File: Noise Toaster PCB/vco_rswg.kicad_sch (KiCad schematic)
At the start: 21 parts, among them Q1 2N5457, U1 LM324, U2 LM324

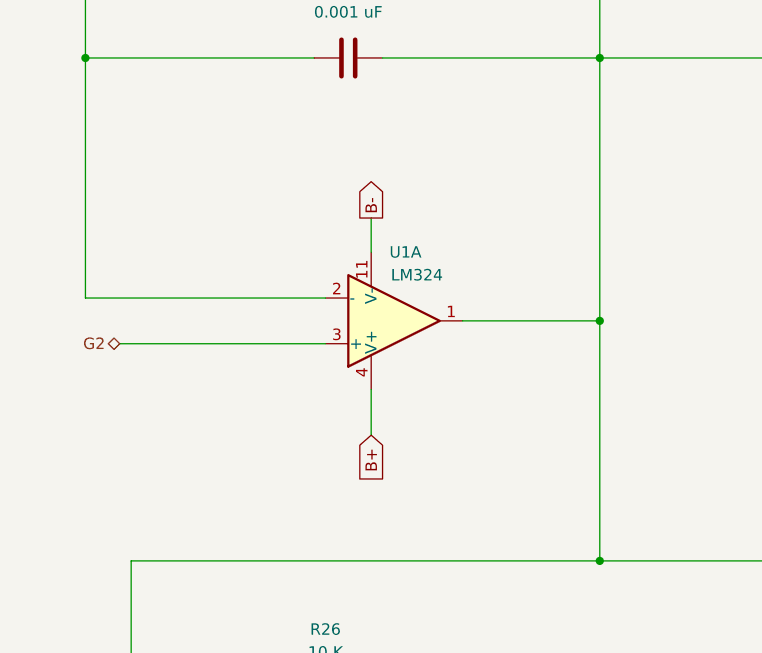
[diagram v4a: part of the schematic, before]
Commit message: applied footprints
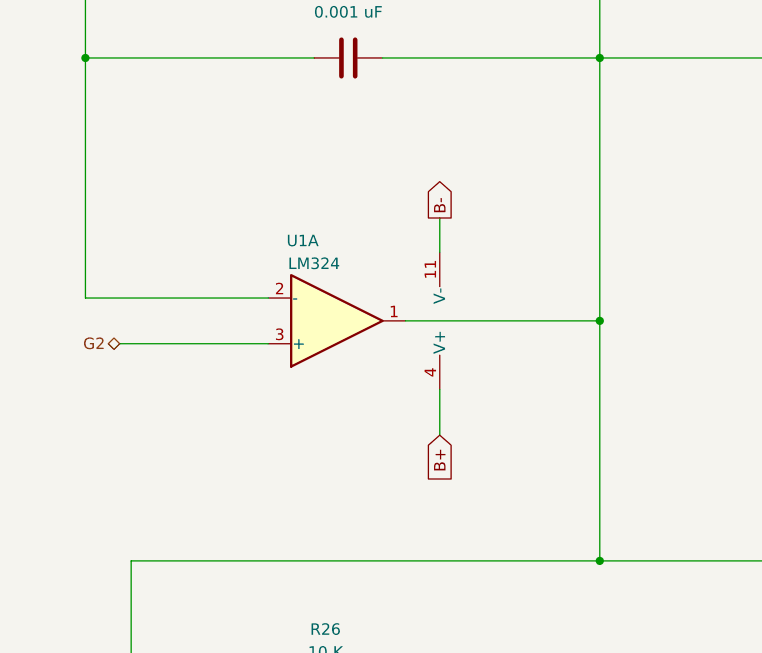
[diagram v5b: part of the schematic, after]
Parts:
- C11, C2, C6: footprint (none) -> Capacitor_THT:C_Disc_D5.1mm_W3.2mm_P5.00mm
- D1: footprint (none) -> Diode_THT:D_DO-35_SOD27_P7.62mm_Horizontal
- Q1: footprint (none) -> Package_TO_SOT_THT:TO-92_Inline
- R12, R17, R18, R24, R26, R30, R31, R32, R5, R6, R7: footprint (none) -> Resistor_THT:R_Axial_DIN0207_L6.3mm_D2.5mm_P10.16mm_Horizontal
- U1, U2: footprint (none) -> Package_DIP:DIP-14_W7.62mm_Socket
- X4: footprint (none) -> Connector_PinHeader_1.00mm:PinHeader_1x01_P1.00mm_Vertical
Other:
- moved on the sheet: U1A
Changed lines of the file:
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@@
     (stroke (width 0) (type default))
   )
-  (wire (pts (xy 63.5 100.33) (xy 63.5 105.41))
+  (wire (pts (xy 71.12 100.33) (xy 71.12 105.41))
     (stroke (width 0) (type default))
   )
@@
     (stroke (width 0) (type default))
   )
-  (wire (pts (xy 73.66 92.71) (xy 88.9 92.71))
+  (wire (pts (xy 67.31 92.71) (xy 88.9 92.71))
     (stroke (width 0) (type default))
   )
@@
     (stroke (width 0) (type default))
   )
-  (wire (pts (xy 35.56 95.25) (xy 58.42 95.25))
+  (wire (pts (xy 35.56 95.25) (xy 52.07 95.25))
     (stroke (width 0) (type default))
   )
@@
     (stroke (width 0) (type default))
   )
-  (wire (pts (xy 31.75 90.17) (xy 58.42 90.17))
+  (wire (pts (xy 31.75 90.17) (xy 52.07 90.17))
     (stroke (width 0) (type default))
   )
@@
     (stroke (width 0) (type default))
   )
-  (wire (pts (xy 63.5 81.28) (xy 63.5 85.09))
+  (wire (pts (xy 71.12 81.28) (xy 71.12 85.09))
     (stroke (width 0) (type default))
   )
@@
     )
   )
-  (global_label "B-" (shape output) (at 63.5 81.28 90) (fields_autoplaced)
+  (global_label "B-" (shape output) (at 71.12 81.28 90) (fields_autoplaced)
     (effects (font (size 1.27 1.27)) (justify left))
-    (property "Intersheetrefs" "${INTERSHEET_REFS}" (at 63.5 75.4524 90)
+    (property "Intersheetrefs" "${INTERSHEET_REFS}" (at 71.12 75.4524 90)
       (effects (font (size 1.27 1.27)) (justify left) hide)
     )
   )
-  (global_label "B+" (shape input) (at 63.5 105.41 270) (fields_autoplaced)
+  (global_label "B+" (shape input) (at 71.12 105.41 270) (fields_autoplaced)
     (effects (font (size 1.27 1.27)) (justify right))
-    (property "Intersheetrefs" "${INTERSHEET_REFS}" (at 63.5 111.2376 90)
+    (property "Intersheetrefs" "${INTERSHEET_REFS}" (at 71.12 111.2376 90)
       (effects (font (size 1.27 1.27)) (justify right) hide)
     )
@@
       (effects (font (size 1.27 1.27)))
     )
-    (property "Footprint" "" (at 95.25 143.51 0)
+    (property "Footprint" "Package_DIP:DIP-14_W7.62mm_Socket" (at 95.25 143.51 0)
       (effects (font (size 1.27 1.27)) hide)
     )
@@
       (effects (font (size 1.27 1.27)))
     )
-    (property "Footprint" "" (at 246.38 133.35 0)
+    (property "Footprint" "Connector_PinHeader_1.00mm:PinHeader_1x01_P1.00mm_Vertical" (at 246.38 133.35 0)
       (effects (font (size 1.27 1.27)) hide)
     )
@@
       (effects (font (size 1.27 1.27)))
     )
-    (property "Footprint" "" (at 196.85 63.5 0)
+    (property "Footprint" "Package_DIP:DIP-14_W7.62mm_Socket" (at 196.85 63.5 0)
       (effects (font (size 1.27 1.27)) hide)
     )
@@
       (effects (font (size 1.27 1.27)))
     )
-    (property "Footprint" "" (at 58.42 150.368 90)
+    (property "Footprint" "Resistor_THT:R_Axial_DIN0207_L6.3mm_D2.5mm_P10.16mm_Horizontal" (at 58.42 150.368 90)
       (effects (font (size 1.27 1.27)) hide)
     )
@@
       (effects (font (size 1.27 1.27)))
     )
-    (property "Footprint" "" (at 123.19 27.178 90)
+    (property "Footprint" "Resistor_THT:R_Axial_DIN0207_L6.3mm_D2.5mm_P10.16mm_Horizontal" (at 123.19 27.178 90)
       (effects (font (size 1.27 1.27)) hide)
     )
@@
       (effects (font (size 1.27 1.27)))
     )
-    (property "Footprint" "" (at 215.9 103.378 90)
+    (property "Footprint" "Resistor_THT:R_Axial_DIN0207_L6.3mm_D2.5mm_P10.16mm_Horizontal" (at 215.9 103.378 90)
       (effects (font (size 1.27 1.27)) hide)
     )
@@
       (effects (font (size 1.27 1.27)))
     )
-    (property "Footprint" "" (at 158.75 25.4 0)
+    (property "Footprint" "Diode_THT:D_DO-35_SOD27_P7.62mm_Horizontal" (at 158.75 25.4 0)
       (effects (font (size 1.27 1.27)) hide)
     )
@@
       (effects (font (size 1.27 1.27)))
     )
-    (property "Footprint" "" (at 215.9 119.888 90)
+    (property "Footprint" "Resistor_THT:R_Axial_DIN0207_L6.3mm_D2.5mm_P10.16mm_Horizontal" (at 215.9 119.888 90)
       (effects (font (size 1.27 1.27)) hide)
     )
@@
       (effects (font (size 1.27 1.27)))
     )
-    (property "Footprint" "" (at 114.3 95.25 0)
+    (property "Footprint" "Connector_PinHeader_1.00mm:PinHeader_1x01_P1.00mm_Vertical" (at 114.3 95.25 0)
       (effects (font (size 1.27 1.27)) hide)
     )
@@
       (effects (font (size 1.27 1.27)))
     )
-    (property "Footprint" "" (at 203.2 46.228 90)
+    (property "Footprint" "Resistor_THT:R_Axial_DIN0207_L6.3mm_D2.5mm_P10.16mm_Horizontal" (at 203.2 46.228 90)
       (effects (font (size 1.27 1.27)) hide)
     )
@@
       (effects (font (size 1.27 1.27)))
     )
-    (property "Footprint" "" (at 185.42 135.128 90)
+    (property "Footprint" "Resistor_THT:R_Axial_DIN0207_L6.3mm_D2.5mm_P10.16mm_Horizontal" (at 185.42 135.128 90)
       (effects (font (size 1.27 1.27)) hide)
     )
@@
       (effects (font (size 1.27 1.27)))
     )
-    (property "Footprint" "" (at 123.19 39.878 90)
+    (property "Footprint" "Resistor_THT:R_Axial_DIN0207_L6.3mm_D2.5mm_P10.16mm_Horizontal" (at 123.19 39.878 90)
       (effects (font (size 1.27 1.27)) hide)
     )
@@
       (effects (font (size 1.27 1.27)))
     )
-    (property "Footprint" "" (at 58.42 133.858 90)
+    (property "Footprint" "Resistor_THT:R_Axial_DIN0207_L6.3mm_D2.5mm_P10.16mm_Horizontal" (at 58.42 133.858 90)
       (effects (font (size 1.27 1.27)) hide)
     )
@@
       (effects (font (size 1.27 1.27)))
     )
-    (property "Footprint" "" (at 62.23 176.8348 0)
+    (property "Footprint" "Capacitor_THT:C_Disc_D5.1mm_W3.2mm_P5.00mm" (at 62.23 176.8348 0)
       (effects (font (size 1.27 1.27)) hide)
     )
@@
       (effects (font (size 1.27 1.27)))
     )
-    (property "Footprint" "" (at 185.42 149.098 90)
+    (property "Footprint" "Resistor_THT:R_Axial_DIN0207_L6.3mm_D2.5mm_P10.16mm_Horizontal" (at 185.42 149.098 90)
       (effects (font (size 1.27 1.27)) hide)
     )
@@
       (effects (font (size 1.27 1.27)) (justify right))
     )
-    (property "Footprint" "" (at 164.1348 96.52 0)
+    (property "Footprint" "Capacitor_THT:C_Disc_D5.1mm_W3.2mm_P5.00mm" (at 164.1348 96.52 0)
       (effects (font (size 1.27 1.27)) hide)
     )
@@
       (effects (font (size 1.27 1.27)))
     )
-    (property "Footprint" "" (at 64.77 62.5348 0)
+    (property "Footprint" "Capacitor_THT:C_Disc_D5.1mm_W3.2mm_P5.00mm" (at 64.77 62.5348 0)
       (effects (font (size 1.27 1.27)) hide)
     )
@@
     )
   )
-  (symbol (lib_id "Amplifier_Operational:LM324") (at 66.04 92.71 0) (mirror x) (unit 1)
-    (in_bom yes) (on_board yes) (dnp no)
-    (property "Reference" "U1" (at 67.31 85.09 0)
-      (effects (font (size 1.27 1.27)))
-    )
-    (property "Value" "LM324" (at 68.58 87.63 0)
-      (effects (font (size 1.27 1.27)))
-    )
-    (property "Footprint" "" (at 64.77 95.25 0)
-      (effects (font (size 1.27 1.27)) hide)
-    )
-    (property "Datasheet" "http://www.ti.com/lit/ds/symlink/lm2902-n.pdf" (at 67.31 97.79 0)
+  (symbol (lib_id "Amplifier_Operational:LM324") (at 59.69 92.71 0) (mirror x) (unit 1)
+    (in_bom yes) (on_board yes) (dnp no)
+    (property "Reference" "U1" (at 55.88 83.82 0)
+      (effects (font (size 1.27 1.27)))
+    )
+    (property "Value" "LM324" (at 57.15 86.36 0)
+      (effects (font (size 1.27 1.27)))
+    )
+    (property "Footprint" "Package_DIP:DIP-14_W7.62mm_Socket" (at 58.42 95.25 0)
+      (effects (font (size 1.27 1.27)) hide)
+    )
+    (property "Datasheet" "http://www.ti.com/lit/ds/symlink/lm2902-n.pdf" (at 60.96 97.79 0)
       (effects (font (size 1.27 1.27)) hide)
     )
@@
       (effects (font (size 1.27 1.27)))
     )
-    (property "Footprint" "" (at 124.46 65.278 90)
+    (property "Footprint" "Resistor_THT:R_Axial_DIN0207_L6.3mm_D2.5mm_P10.16mm_Horizontal" (at 124.46 65.278 90)
       (effects (font (size 1.27 1.27)) hide)
     )
@@
       (effects (font (size 1.27 1.27)))
     )
-    (property "Footprint" "" (at 58.42 43.18 0)
+    (property "Footprint" "Package_TO_SOT_THT:TO-92_Inline" (at 58.42 43.18 0)
       (effects (font (size 1.27 1.27)) hide)
     )
@@
       (effects (font (size 1.27 1.27)))
     )
-    (property "Footprint" "" (at 127 119.38 0)
+    (property "Footprint" "Connector_PinHeader_1.00mm:PinHeader_1x01_P1.00mm_Vertical" (at 127 119.38 0)
       (effects (font (size 1.27 1.27)) hide)
     )
@@
     )
   )
-  (symbol (lib_id "Amplifier_Operational:LM324") (at 60.96 92.71 180) (unit 5)
-    (in_bom yes) (on_board yes) (dnp no)
-    (property "Reference" "U1" (at 64.77 91.44 0)
+  (symbol (lib_id "Amplifier_Operational:LM324") (at 68.58 92.71 180) (unit 5)
+    (in_bom yes) (on_board yes) (dnp no)
+    (property "Reference" "U1" (at 72.39 91.44 0)
       (effects (font (size 1.27 1.27)) (justify right) hide)
     )
-    (property "Value" "LM324" (at 67.31 96.52 0)
+    (property "Value" "LM324" (at 74.93 96.52 0)
       (effects (font (size 1.27 1.27)) (justify right) hide)
     )
-    (property "Footprint" "" (at 62.23 95.25 0)
-      (effects (font (size 1.27 1.27)) hide)
-    )
-    (property "Datasheet" "http://www.ti.com/lit/ds/symlink/lm2902-n.pdf" (at 59.69 97.79 0)
+    (property "Footprint" "Package_DIP:DIP-14_W7.62mm_Socket" (at 69.85 95.25 0)
+      (effects (font (size 1.27 1.27)) hide)
+    )
+    (property "Datasheet" "http://www.ti.com/lit/ds/symlink/lm2902-n.pdf" (at 67.31 97.79 0)
       (effects (font (size 1.27 1.27)) hide)
     )
@@
       (effects (font (size 1.27 1.27)))
     )
-    (property "Footprint" "" (at 215.9 84.328 90)
-      (effects (font (size 1.27 1.27)) hide)
-    )
+    (property "Footprint" "Resistor_THT:R_Axial_DIN0207_L6.3mm_D2.5mm_P10.16mm_Horizontal" (at 215.9 84.328 90)
+      (effects (font (size 1.27 1.27)) hide)
+    )

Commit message: placed pards of the pcb properly
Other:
- company: http://musicfromouterspace.com/analogsynth_new/NOISETOASTER/NOISETOASTER.php -> Music From Outer Space LLC
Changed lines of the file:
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@@
     (title "VCO - Ramp/Square Wave Generator")
     (rev "0.5")
-    (company "http://musicfromouterspace.com/analogsynth_new/NOISETOASTER/NOISETOASTER.php")
+    (company "Music From Outer Space LLC")
     (comment 1 "Licence: CC-BY-NC-SA")
     (comment 2 "Original Design by Ray Wilson")
-    (comment 3 "Music From Outer Space LLC")
+    (comment 3 "http://musicfromouterspace.com/analogsynth_new/NOISETOASTER/NOISETOASTER.php")
   )
   (junction (at 165.1 118.11) (diameter 0) (color 0 0 0 0)

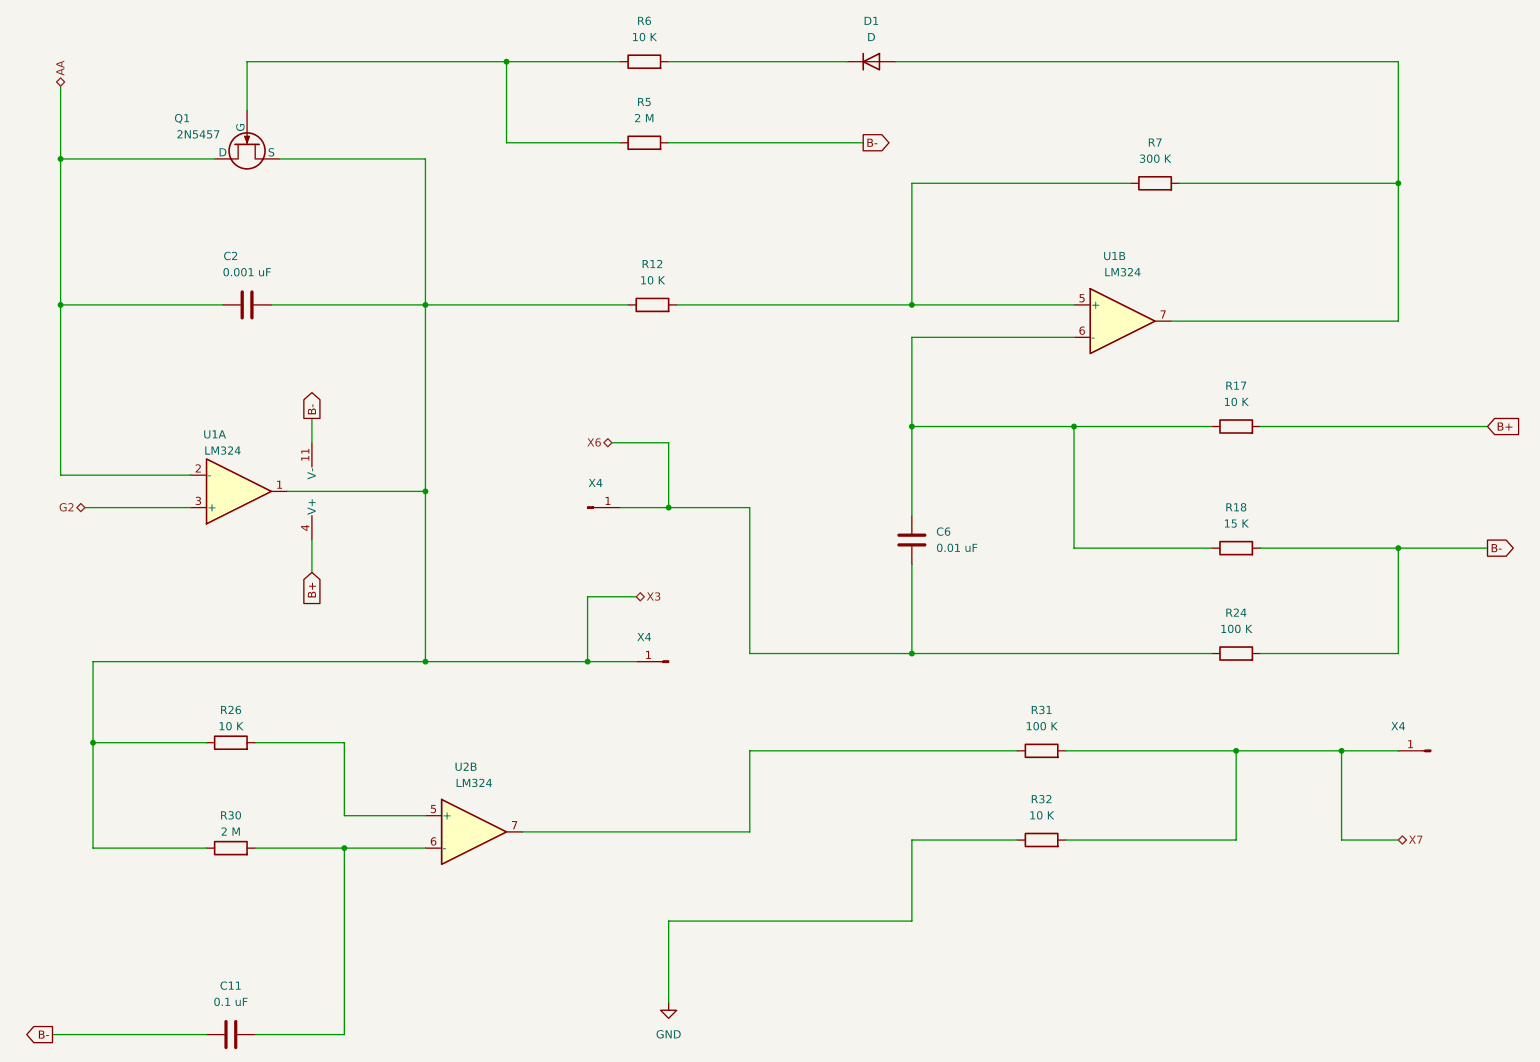
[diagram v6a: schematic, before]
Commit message: changed header pins to groups
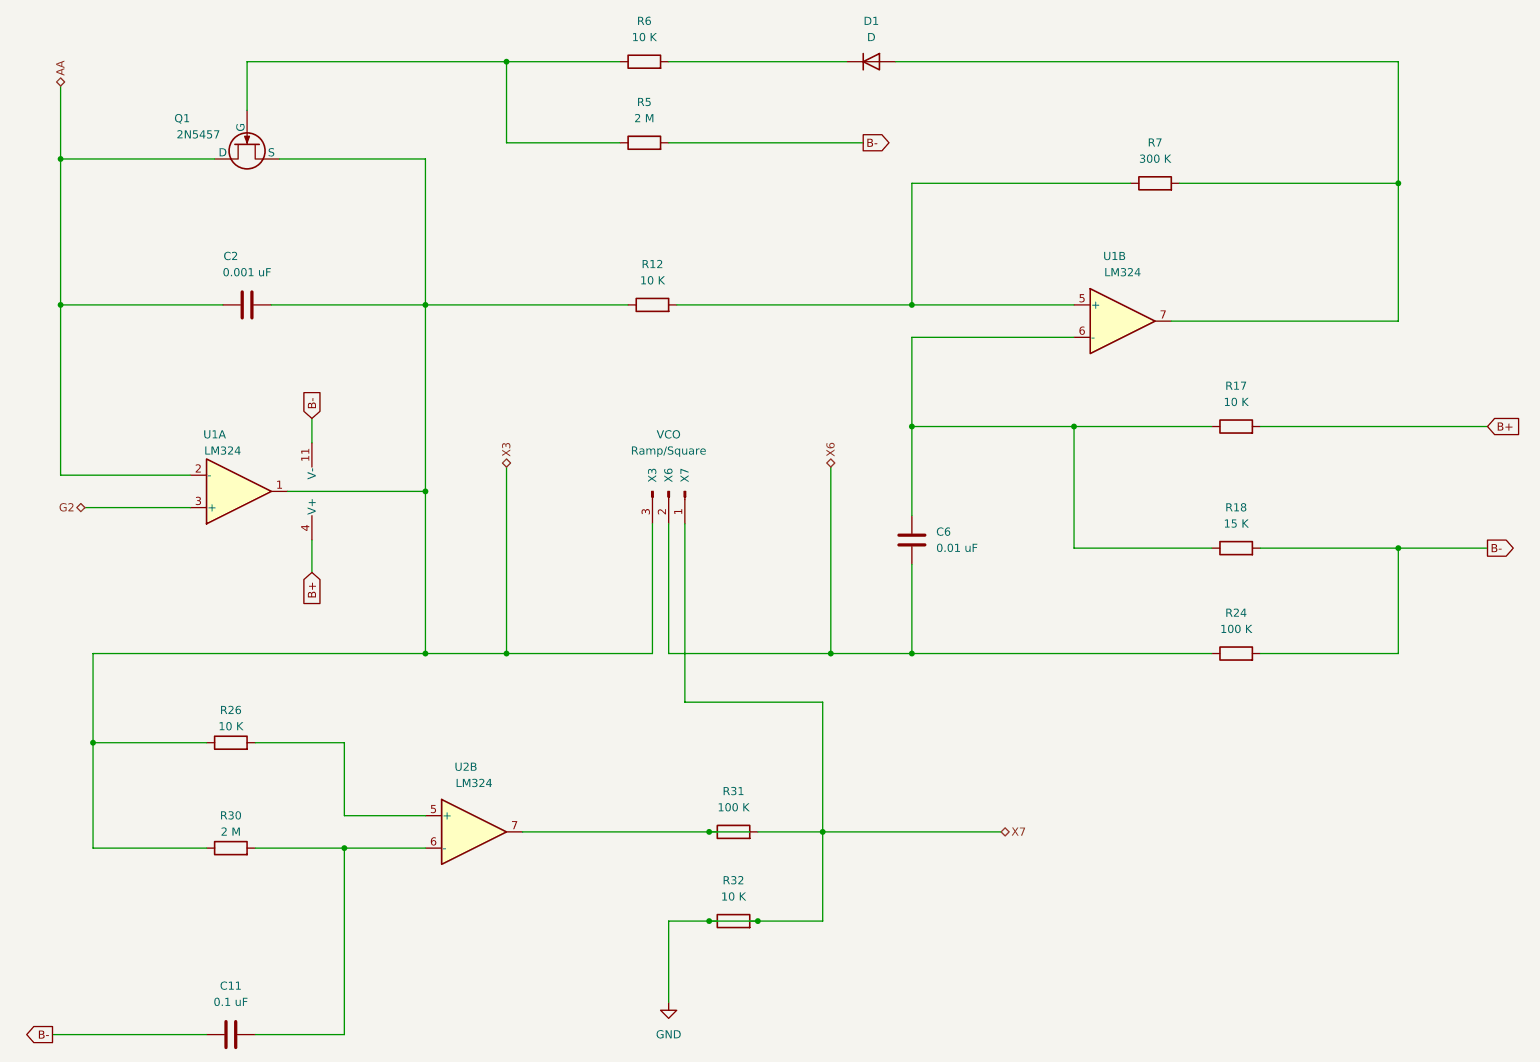
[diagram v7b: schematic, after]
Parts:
- removed X4 (x3): ~, Connector_PinHeader_1.00mm:PinHeader_1x01_P1.00mm_Vertical, symbol Connector:Conn_01x01_Pin
- added J6: VCO, Connector_PinHeader_2.00mm:PinHeader_1x03_P2.00mm_Vertical, symbol Connector:Conn_01x03_Pin
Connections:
- net X7 is gone; now on net GND: R31.2, R32.2
- net GND: now also J6.1 (Pin_1)
- net X3: now also J6.3 (Pin_3)
- net X6: now also J6.2 (Pin_2)
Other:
- moved on the sheet: R31, R32
